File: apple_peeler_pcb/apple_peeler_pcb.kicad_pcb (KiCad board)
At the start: 2 copper layers, 130 parts, among them J1 BM03B-SRSS-TB, J2 BM03B-SRSS-TB, J3 HYC10-HDMIA19-600B, J4 HYC10-HDMIA19-600B, J5 USB_C_Receptacle_USB2.0_16P, Q1 2N7002, Q10 2N7002, Q11 2N7002, Q12 2N7002, Q13 2N7002, Q14 AO3401A, Q15 2N7002, Q16 AO3401A, Q17 2N7002, Q18 2N7002, Q2 2N7002, Q3 2N7002, Q4 2N7002, Q5 2N7002, Q6 2N7002, Q7 2N7002, Q8 2N7002, Q9 2N7002, SW1 SPST BTN, SW2 SPST BTN, SW3 SPST BTN, U1 W25Q16JVSS, U2 RP2040, U3 4066, U4 TPS562242, Y1 12MHz

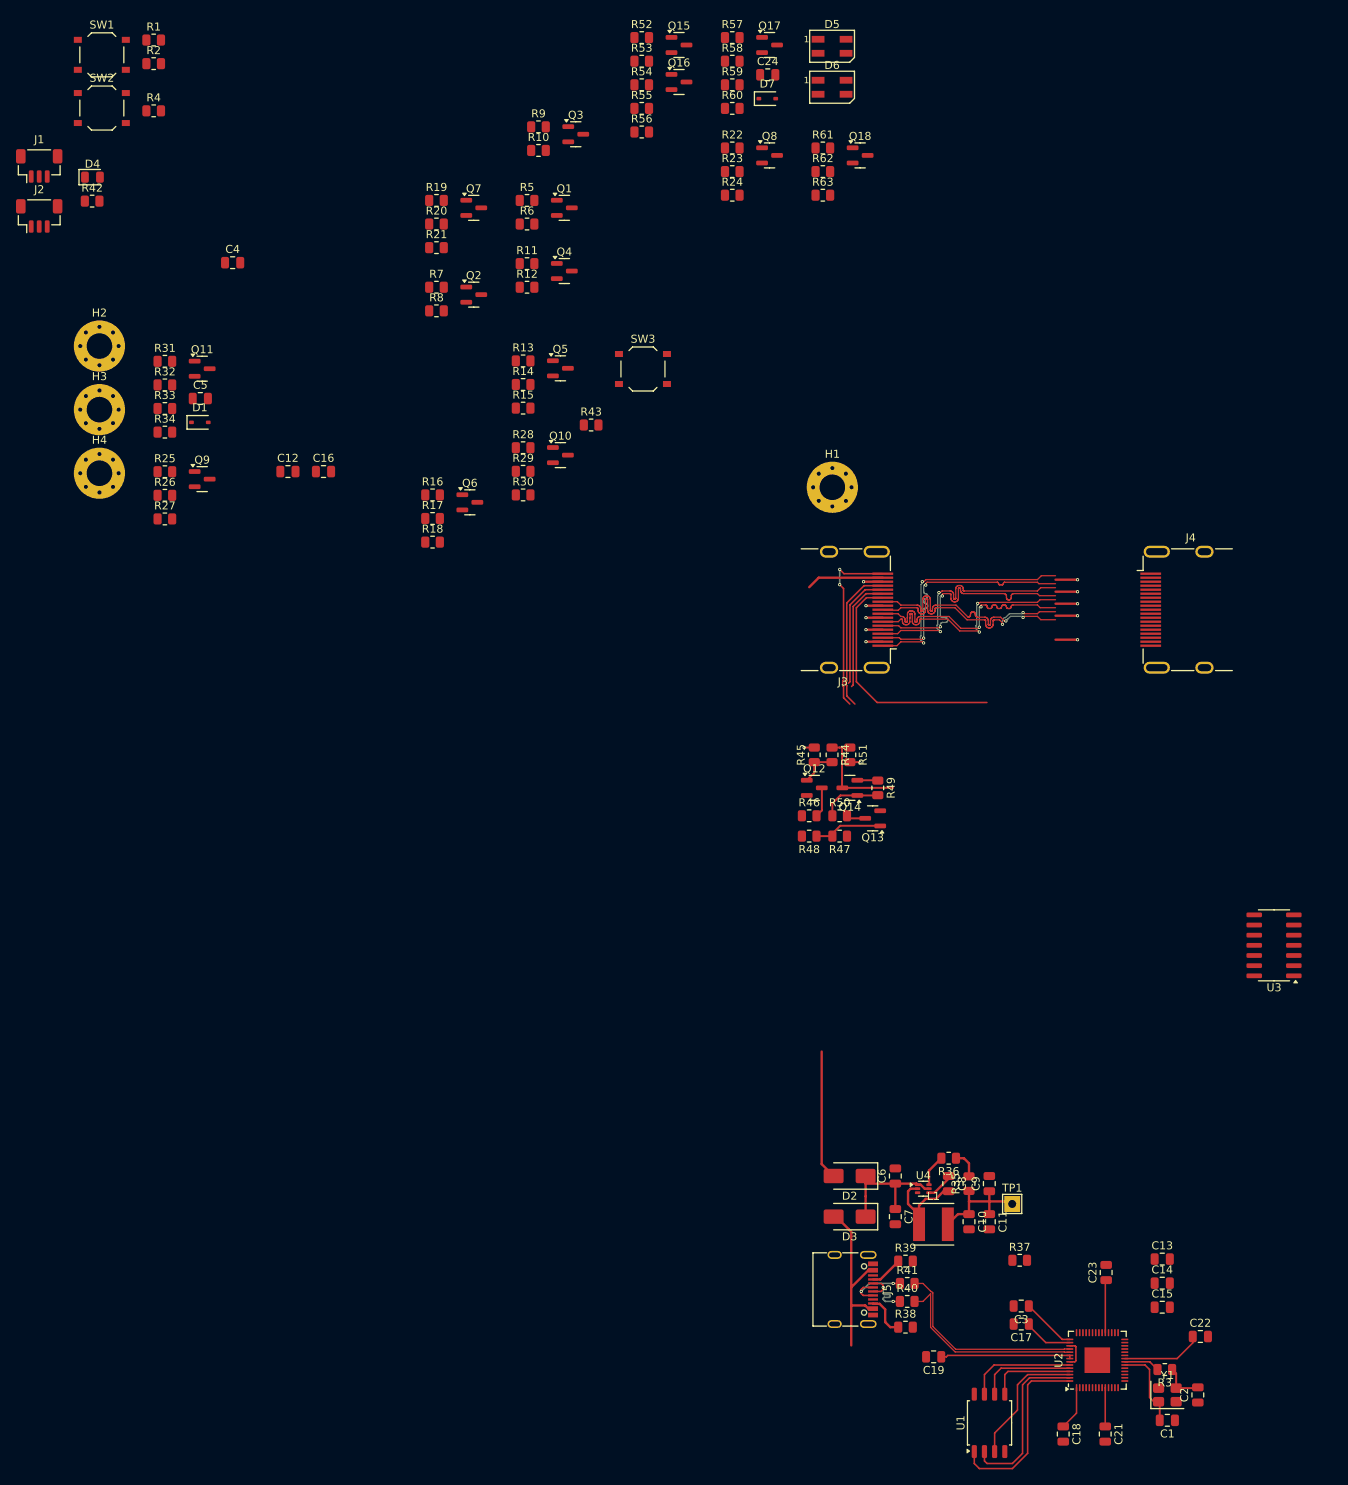
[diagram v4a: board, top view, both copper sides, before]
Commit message: route hdmi traces
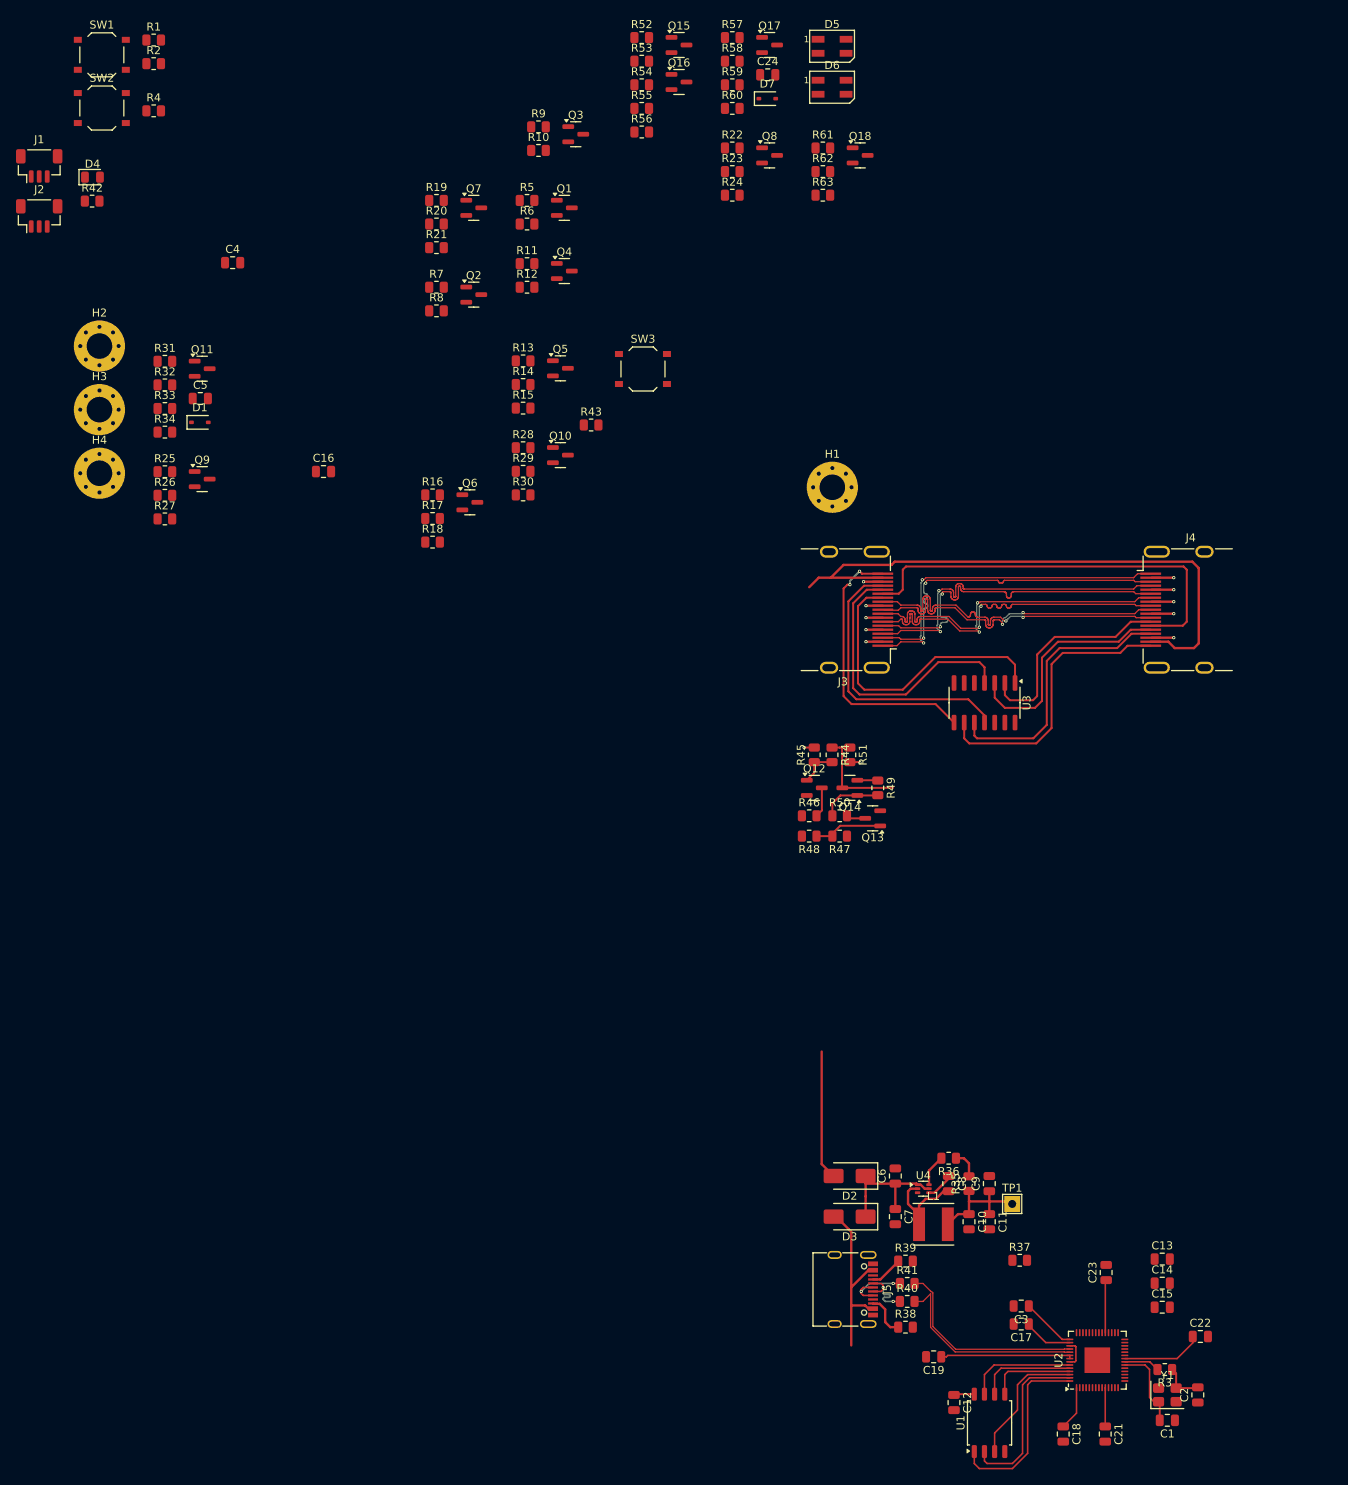
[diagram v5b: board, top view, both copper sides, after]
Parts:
- moved C12 143.1 mm to (172.4, 205.1), turned to -90 degrees
- moved U3 47.2 mm to (176.2, 117.6), turned to -90 degrees
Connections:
- U3 pad 1: /HDMI passthrough/Bidir level shifter/L_5V -> /HDMI passthrough/CEC interface/CEC_LINE
- U3 pad 10: /HDMI passthrough/CEC interface1/CEC_LINE -> /HDMI passthrough/Bidir level shifter2/L_5V
- U3 pad 11: /HDMI passthrough/CEC interface/CEC_LINE -> /HDMI passthrough/Bidir level shifter/L_5V
- U3 pad 12: /HDMI passthrough/Pullup level shifter3/OUT_5V -> /HDMI passthrough/Pullup level shifter/OUT_5V
- U3 pad 13: /HDMI passthrough/Pullup level shifter/OUT_5V -> /HDMI passthrough/Pullup level shifter3/OUT_5V
- U3 pad 2: /HDMI passthrough/Bidir level shifter2/L_5V -> /HDMI passthrough/CEC interface1/CEC_LINE
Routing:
- net /HDMI passthrough/HDMI_VCC: track 25.9 -> 89.0 mm
- net /HDMI passthrough/HDMI connectors/ARC_SINK: track 14.5 -> 52.2 mm
- net /HDMI passthrough/HDMI connectors/HPD_SINK: track 0.00 -> 35.3 mm
- net /HDMI passthrough/Bidir level shifter2/L_5V: track 0.00 -> 33.9 mm
- net /HDMI passthrough/Bidir level shifter3/L_5V: track 0.00 -> 29.1 mm
- net /HDMI passthrough/CEC interface1/CEC_LINE: track 0.00 -> 27.1 mm
- net /HDMI passthrough/Bidir level shifter1/L_5V: track 14.8 -> 35.7 mm
- net /HDMI passthrough/Bidir level shifter/L_5V: track 18.6 -> 35.5 mm
- net /HDMI passthrough/HDMI connectors/D2-: track 30.2 -> 42.4 mm
- net /HDMI passthrough/HDMI connectors/D1-: track 31.1 -> 43.4 mm
- net /HDMI passthrough/HDMI connectors/D1+: track 30.1 -> 42.4 mm
- net /HDMI passthrough/HDMI connectors/D2+: track 30.3 -> 42.5 mm
- net /HDMI passthrough/HDMI connectors/D0+: track 30.0 -> 42.0 mm
- net /HDMI passthrough/HDMI connectors/CK+: track 29.6 -> 41.6 mm
- net /HDMI passthrough/HDMI connectors/D0-: track 30.1 -> 42.0 mm
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
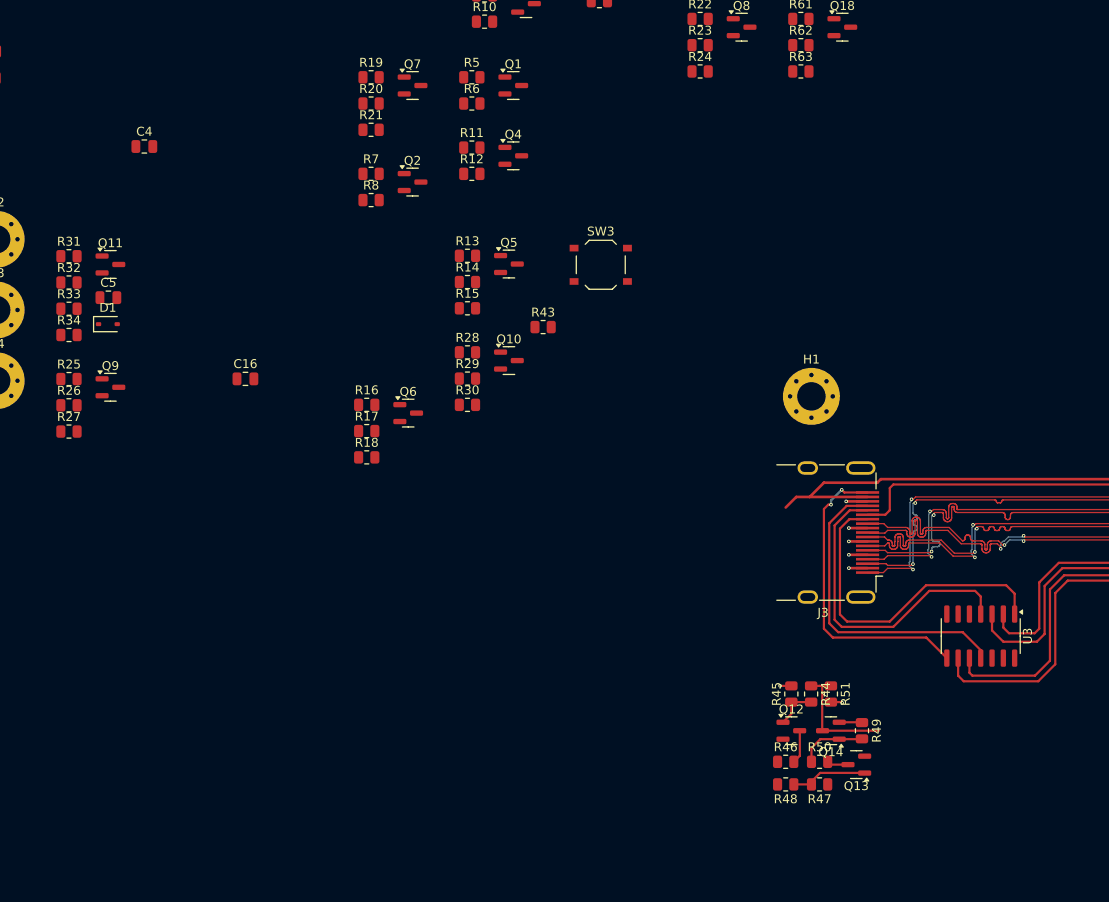
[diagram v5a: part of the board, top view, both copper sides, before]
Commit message: route side A level shifters
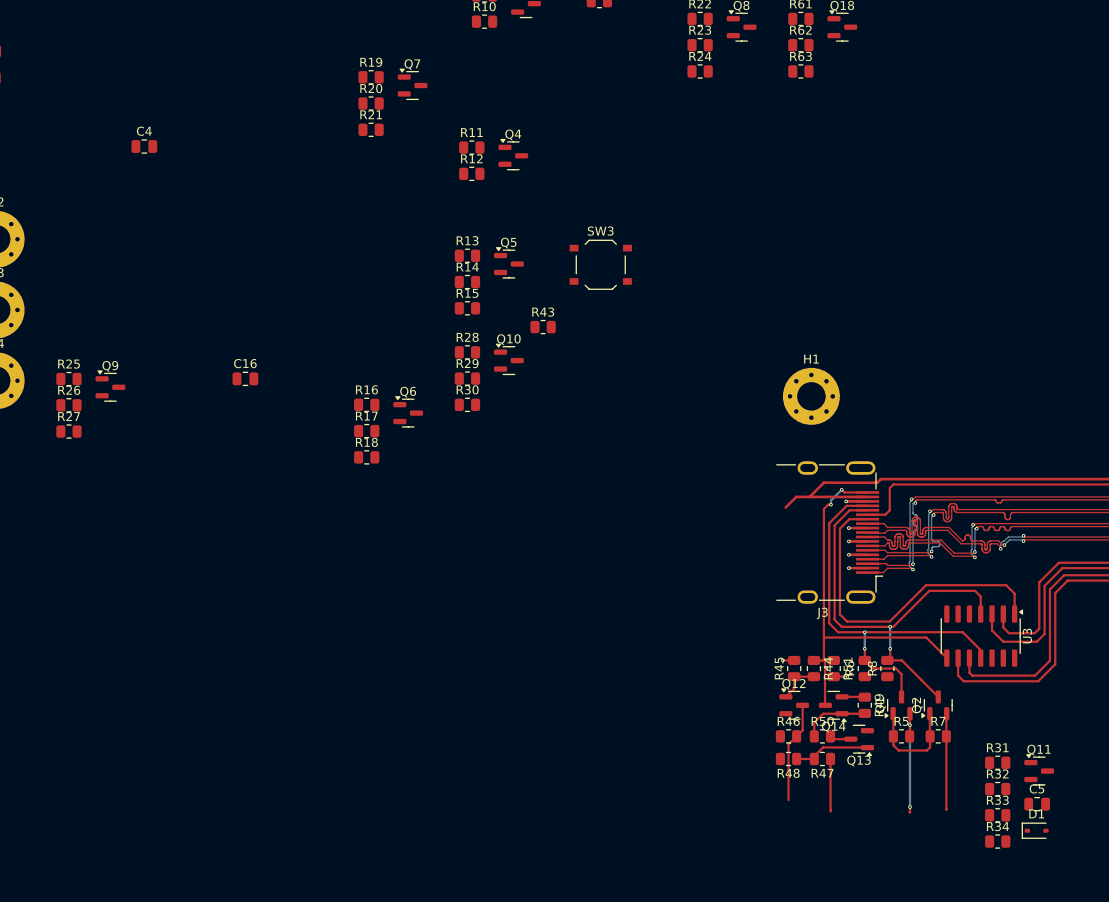
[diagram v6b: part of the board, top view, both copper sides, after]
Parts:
- moved C5 118.9 mm to (182.6, 136.5)
- moved D1 118.9 mm to (182.5, 139.5)
- moved Q11 118.9 mm to (182.8, 132.8)
- moved R31 118.9 mm to (178.1, 131.9)
- moved R32 118.9 mm to (178.1, 134.8)
- moved R33 118.9 mm to (178.1, 137.8)
- moved R34 118.9 mm to (178.1, 140.7)
- moved R7 89.8 mm to (171.4, 128.9)
- moved R5 88.4 mm to (167.3, 128.9)
- moved Q2 83.3 mm to (171.4, 125.4), turned to 90 degrees
- moved Q1 82.2 mm to (167.3, 125.4), turned to 90 degrees
- moved R8 78.3 mm to (165.7, 121.3), turned to 90 degrees
- moved R6 77.3 mm to (163.2, 121.3), turned to 90 degrees
- moved Q12 2.88 mm to (155.3, 125.4)
- moved Q13 2.88 mm to (162.6, 129.2)
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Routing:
- net /HDMI passthrough/SDA_SRC_3V3: track 0.00 -> 12.4 mm, vias 0 -> 2
- net +3.3V: track 66.9 -> 78.8 mm
- net /HDMI passthrough/Bidir level shifter1/L_5V: track 35.7 -> 47.0 mm, vias 0 -> 2
- net /HDMI passthrough/SCL_SRC_3V3: track 0.00 -> 10.8 mm
- net /HDMI passthrough/Bidir level shifter/L_5V: track 35.5 -> 46.0 mm, vias 0 -> 2
- net /HDMI passthrough/HPD_SRC_MON: track 3.78 -> 11.3 mm
- net /HDMI passthrough/HPD_SRC_ASSERT: track 0.00 -> 5.94 mm
- net /HDMI passthrough/HDMI connectors/HPD_SRC: track 48.4 -> 45.3 mm

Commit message: cec interface A
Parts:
- moved D1 14.3 mm to (178.8, 125.7), turned to -90 degrees
- moved R34 11.3 mm to (181.3, 129.9), turned to 90 degrees
- moved C5 10.9 mm to (181.3, 125.7), turned to 90 degrees
- moved Q11 10.3 mm to (175.6, 125.4), turned to 90 degrees
- moved R33 7.97 mm to (179.1, 129.9), turned to 90 degrees
- moved R32 5.13 mm to (176.8, 129.9), turned to -90 degrees
- moved R31 4.05 mm to (174.6, 129.9), turned to 90 degrees
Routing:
- net /HDMI passthrough/CEC interface/CEC_LINE: track 37.5 -> 70.0 mm, vias 0 -> 4
- net +3.3V: track 78.8 -> 88.7 mm
- net /HDMI passthrough/CEC_SRC_PULLDOWN: track 0.00 -> 6.39 mm
- net Net-(D1-A): track 0.00 -> 5.27 mm
- net Net-(Q11-G): track 0.00 -> 4.82 mm
- net /HDMI passthrough/CEC_SRC_MON: track 0.00 -> 2.26 mm
- net /HDMI passthrough/SCL_SRC_3V3: track 10.8 -> 12.2 mm, vias 0 -> 2

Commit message: AAAAAAAAAAAAAAAAAAAAAAAAAAAAAAAAAAAAAAAAAAAAAAAAAAA
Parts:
- moved R19 107.5 mm to (192.5, 121.0), turned to 180 degrees
- moved R20 104.4 mm to (192.5, 118.8)
- moved R21 100.8 mm to (189.5, 119.8), turned to -90 degrees
- moved Q7 99.8 mm to (192.5, 115.2), turned to 90 degrees
- moved Q10 90.5 mm to (201.7, 131.8)
- moved R28 90.5 mm to (197.0, 130.9)
- moved R29 90.5 mm to (197.0, 133.8)
- moved R30 90.5 mm to (197.0, 136.8)
- moved R13 86.8 mm to (184.5, 131.4), turned to 180 degrees
- moved R16 84.3 mm to (186.2, 121.0), turned to 180 degrees
- moved R18 84.3 mm to (189.5, 115.8), turned to 90 degrees
- moved R14 83.6 mm to (184.5, 129.2)
- moved R17 82.6 mm to (186.2, 118.8)
- moved R15 82.6 mm to (188.0, 125.5), turned to 90 degrees
- moved Q5 78.8 mm to (184.5, 125.4), turned to 90 degrees
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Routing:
- net /HDMI passthrough/Pullup level shifter2/OUT_5V: track 0.00 -> 38.2 mm, vias 0 -> 2
- net /HDMI passthrough/Pullup level shifter1/OUT_5V: track 0.00 -> 25.9 mm, vias 0 -> 2
- net /HDMI passthrough/Pullup level shifter3/OUT_5V: track 0.00 -> 25.5 mm
- net /HDMI passthrough/SCL_BRIDGE: track 0.00 -> 16.5 mm, vias 0 -> 1
- net /HDMI passthrough/Pullup level shifter/OUT_5V: track 0.00 -> 13.9 mm, vias 0 -> 2
- net /HDMI passthrough/Bidir level shifter2/L_5V: track 33.9 -> 46.4 mm
- net /HDMI passthrough/HDMI connectors/HPD_SINK: track 35.3 -> 47.8 mm
- net /HDMI passthrough/SDA_BRIDGE: track 0.00 -> 5.73 mm
- net Net-(Q5-G): track 0.00 -> 5.11 mm
- net Net-(Q7-G): track 0.00 -> 4.83 mm
- net Net-(Q6-G): track 0.00 -> 4.83 mm
- net GND: track 27.5 -> 29.7 mm, vias 12 -> 14
- net /HDMI passthrough/Bidir level shifter3/L_5V: track 29.1 -> 28.4 mm
